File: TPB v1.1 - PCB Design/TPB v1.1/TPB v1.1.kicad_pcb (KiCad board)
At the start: 2 copper layers, 29.5 x 44.7 mm, 28 parts, among them CN1 TYPE-C-31-M-12, J1 Conn_02x03_Top_Bottom, Q1 BC847, Q2 BC847, SW1 SW_Push, SW2 SW_Push, U1 CH340C, U2 AMS1117-3.3

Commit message: PCB Layout v1
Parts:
- C2, C3, R6, R7, U1: moved to B.Cu
- J1: value Conn_02x03_Top_Bottom -> ~
- moved SW2 126.7 mm to (49.2, 175.3), turned to 90 degrees
- moved R5 125.1 mm to (43.4, 180.6), turned to 180 degrees
- moved U1 117.9 mm to (55.8, 172.5), turned to 90 degrees
- moved SW1 116.1 mm to (49.2, 164.9)
- moved R6 111.4 mm to (62.5, 179.0), turned to -90 degrees
- moved R7 110.6 mm to (59.8, 179.0), turned to -90 degrees
- moved R3 110.1 mm to (43.4, 172.6)
- moved R4 105.8 mm to (43.4, 169.5), turned to 180 degrees
- moved Q1 105.6 mm to (43.4, 165.5)
- moved R2 103.5 mm to (43.4, 161.5), turned to 180 degrees
- moved C3 97.5 mm to (59.8, 166.4), turned to 90 degrees
- moved R1 93.1 mm to (48.3, 188.0)
- moved C1 92.4 mm to (48.3, 184.2)
- moved D3 47.5 mm to (43.4, 154.0), turned to 180 degrees
- moved R10 47.4 mm to (43.4, 157.5)
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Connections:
- CN1 pad A6: /USB -> /USB_P
- CN1 pad A7: /USB -> /USB_N
- CN1 pad B6: /USB -> /USB_P
- CN1 pad B7: /USB -> /USB_N
- J1 pad 2: /IO0 -> /TX
- J1 pad 3: GND -> /IO0
- J1 pad 4: /TX -> /RX
- J1 pad 5: /RX -> GND
- U1 pad 5: /USB -> /USB_P
- U1 pad 6: /USB -> /USB_N
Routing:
- net +3V3: track 0.00 -> 103.2 mm, vias 0 -> 7
- net GND: track 23.6 -> 125.8 mm, vias 0 -> 4
- net +5V: track 6.86 -> 62.6 mm, vias 0 -> 2
- net /RTS: track 0.00 -> 46.2 mm, vias 0 -> 1
- net /RX: track 0.00 -> 43.8 mm, vias 0 -> 1
- net /TX: track 0.00 -> 43.6 mm, vias 0 -> 1
- net /EN: track 7.20 -> 39.7 mm
- net /IO0: track 7.20 -> 36.2 mm, vias 0 -> 1
- net /DTR: track 0.00 -> 28.6 mm, vias 0 -> 1
- net Earth: track 0.00 -> 26.4 mm
- net /USB_P: track 0.00 -> 11.2 mm, vias 0 -> 1
- net /USB_N: track 0.00 -> 10.2 mm, vias 0 -> 1
- net Net-(U1-TXD): track 0.00 -> 6.02 mm
- net Net-(Q2-B): track 0.00 -> 4.52 mm
- net Net-(U1-RXD): track 0.00 -> 4.13 mm
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
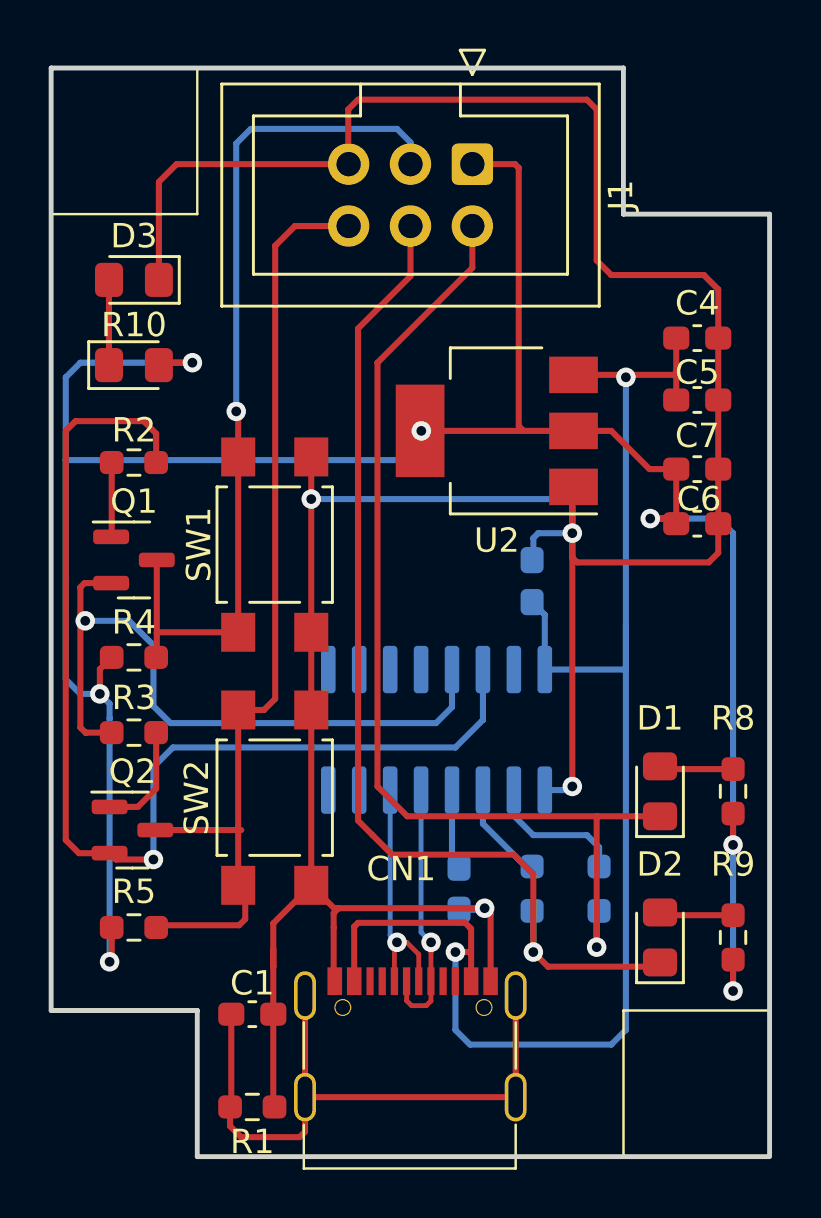
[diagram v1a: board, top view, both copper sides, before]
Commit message: Board Outline, Polygon and 3D of Buttons Added
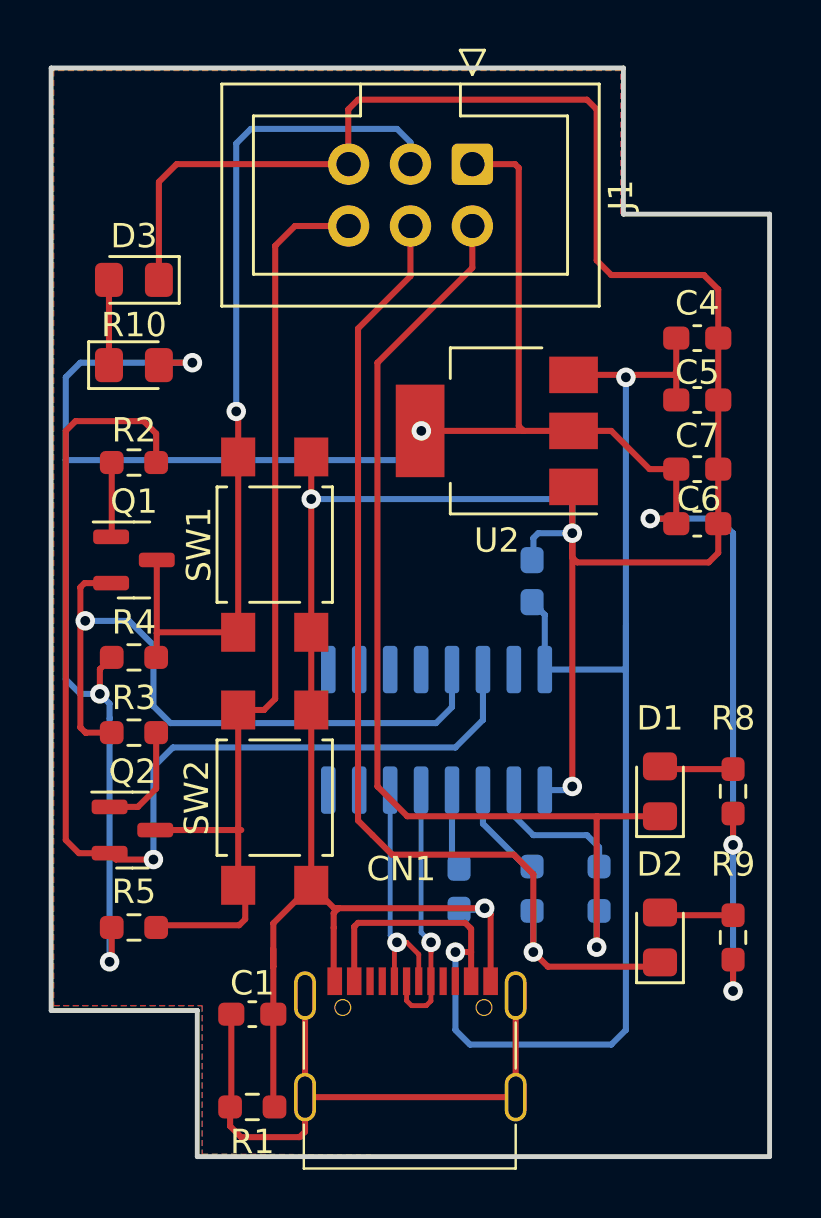
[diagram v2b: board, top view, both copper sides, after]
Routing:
- added copper zone on B.Cu, net GND
- added copper zone on F.Cu, net GND
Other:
- outline, holes or cut-outs redrawn
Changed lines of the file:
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@@
       (layer "B.Paste" (type "Bottom Solder Paste"))
       (layer "B.SilkS" (type "Bottom Silk Screen"))
-      (copper_finish "None")
+      (copper_finish "HAL lead-free")
       (dielectric_constraints no)
+      (edge_connector yes)
     )
     (pad_to_mask_clearance 0)
@@
       (rotate (xyz 0 0 0))
     )
+    (model "${RK_3D}/TL3305AF160QG--3DModel-STEP-520916.STEP"
+      (offset (xyz 0 0 0))
+      (scale (xyz 1 1 1))
+      (rotate (xyz 0 0 0))
+    )
   )
   (footprint "Resistor_SMD:R_0603_1608Metric_Pad0.98x0.95mm_HandSolder" (layer "F.Cu")
@@
     (pad "2" smd rect (at 3.6 1.5 90) (size 1.6 1.4) (layers "F.Cu" "F.Paste" "F.Mask")
       (net 1 "GND") (pinfunction "2") (pintype "passive"))
-    (model "${KICAD6_3DMODEL_DIR}/Button_Switch_SMD.3dshapes/SW_SPST_TL3305C.wrl"
+    (model "${KICAD6_3DMODEL_DIR}/Button_Switch_SMD.3dshapes/SW_SPST_TL3305C.wrl" hide
+      (offset (xyz 0 0 0))
+      (scale (xyz 1 1 1))
+      (rotate (xyz 0 0 0))
+    )
+    (model "${RK_3D}/TL3305AF160QG--3DModel-STEP-520916.STEP"
       (offset (xyz 0 0 0))
       (scale (xyz 1 1 1))
@@
     (fp_line (start 4.7 11.8) (end -4 11.8)
       (stroke (width 0.1) (type default)) (layer "F.SilkS"))
-    (pad "" np_thru_hole circle (at -2.4 5.19) (size 0.7 0.7) (drill oval 0.6) (layers "F&B.Cu" "*.Mask"))
-    (pad "" np_thru_hole circle (at 3.4 5.19) (size 0.7 0.7) (drill oval 0.6) (layers "F&B.Cu" "*.Mask"))
+    (pad "" np_thru_hole circle (at -2.4 5.19) (size 0.7 0.7) (drill oval 0.6) (layers "*.Cu" "*.Mask"))
+    (pad "" np_thru_hole circle (at 3.4 5.19) (size 0.7 0.7) (drill oval 0.6) (layers "*.Cu" "*.Mask"))
     (pad "A1/B12" smd trapezoid (at -2.73 4.11) (size 0.6 1.14) (layers "F.Cu" "F.Paste" "F.Mask")
       (net 1 "GND") (pinfunction "GND") (pintype "power_in") (thermal_bridge_angle 45))
@@
     )
   )
-  (gr_rect (start 40 145.3) (end 46 151.3)
-    (stroke (width 0.1) (type default)) (fill none) (layer "F.SilkS"))
-  (gr_rect (start 63.5 184) (end 69.5 190)
-    (stroke (width 0.1) (type default)) (fill none) (layer "F.SilkS"))
   (gr_line (start 40 184) (end 40 145.3)
     (stroke (width 0.2) (type default)) (layer "Edge.Cuts"))
   (gr_line (start 63.5 145.3) (end 40 145.3)
     (stroke (width 0.2) (type default)) (layer "Edge.Cuts"))
-  (gr_line (start 69.5 151.3) (end 69.5 189.9)
+  (gr_line (start 69.5 151.3) (end 69.5 190)
     (stroke (width 0.2) (type default)) (layer "Edge.Cuts"))
   (gr_line (start 40 184) (end 46 184)
@@
   (segment (start 53.92 180.92) (end 53.92 174.95) (width 0.2) (layer "B.Cu") (net 31))
   (segment (start 54.2 181.2) (end 53.92 180.92) (width 0.2) (layer "B.Cu") (net 31))
+  (zone (net 1) (net_name "GND") (layers "F&B.Cu") (name "GND") (hatch none 0.5)
+    (connect_pads (clearance 0.5))
+    (min_thickness 0.25) (filled_areas_thickness no)
+    (fill yes (thermal_gap 0.5) (thermal_bridge_width 0.5) (island_removal_mode 1) (island_area_min 10))
+    (polygon
+      (pts
+        (xy 69.5 190)
+        (xy 69.5 151.3)
+        (xy 63.4 151.3)
+        (xy 63.4 145.4)
+        (xy 40.1 145.4)
+        (xy 40.1 183.8)
+        (xy 46.2 183.8)
+        (xy 46.2 189.9)
+      )
+    )
+  )
 )

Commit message: Pcb Design Complated
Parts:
- added G***: LOGO, RK_Graphics:RK_Logo_10x10mm, F.Cu at (58.3, 169.7)
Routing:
- net +3V3: track 103.2 -> 103.7 mm, vias 7 -> 12
- net GND: vias 4 -> 28
- added copper zone on B.Cu, net +3V3
- added copper zone on F.Cu, net +3V3
- added copper zone on F.Cu, net +5V
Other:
- board text added: "3V3"
- board text added: "EN"
- board text added: "GND"
- board text added: "IO0"
- board text added: "RX"
- board text added: "TPB v1.1"
- board text added: "TX"

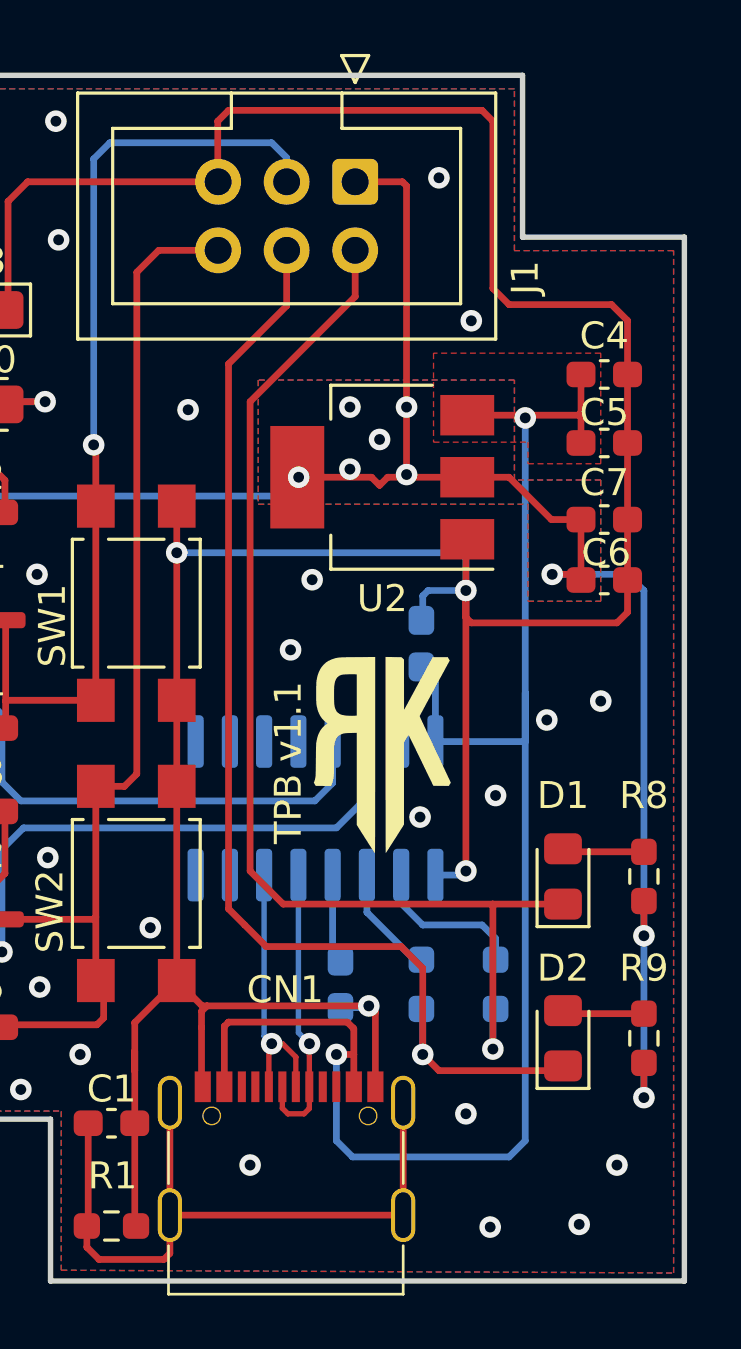
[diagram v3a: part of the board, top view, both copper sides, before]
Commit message: DRC Errs Solved
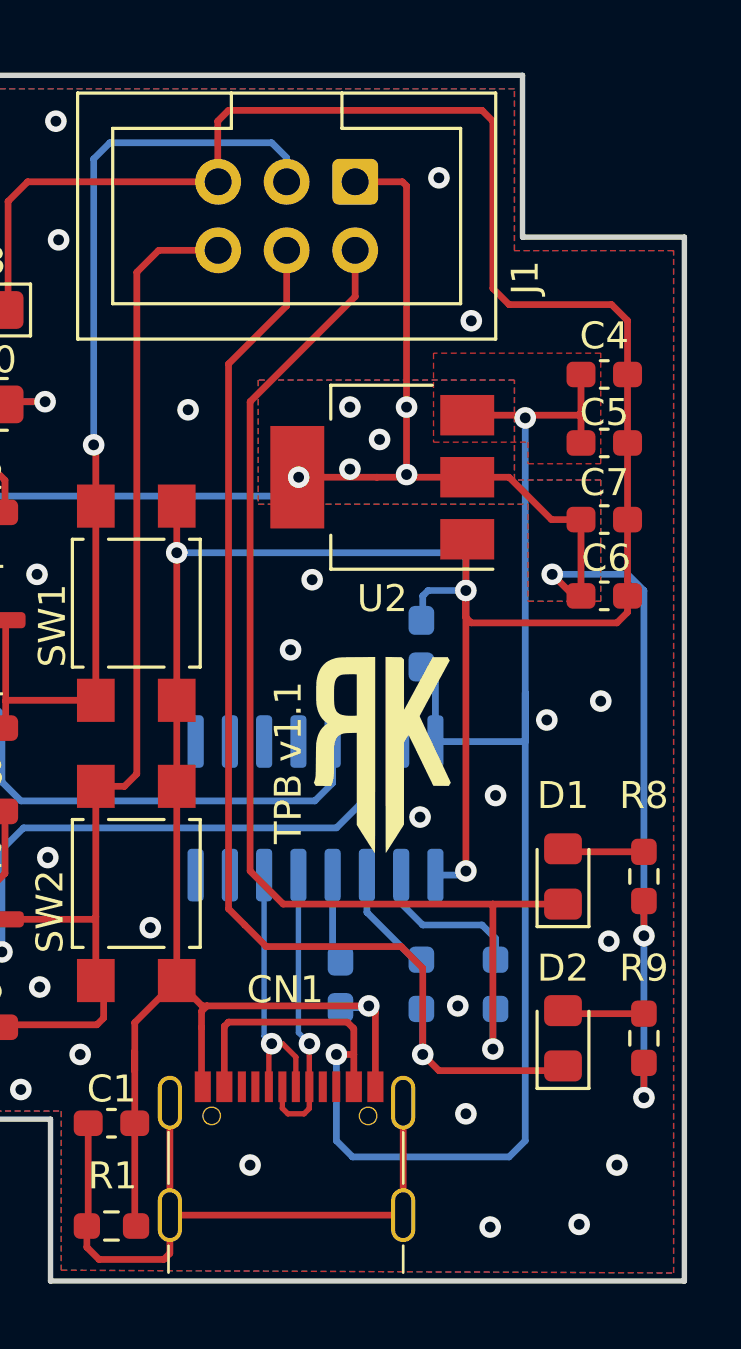
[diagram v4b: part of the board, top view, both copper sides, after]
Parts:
- moved C6 0.59 mm to (66.5, 164.6)
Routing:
- net +3V3: track 103.7 -> 104.3 mm
- net GND: vias 28 -> 30
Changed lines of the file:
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@@
         (effects (font (size 1 1) (thickness 0.15)))
     )
-    (fp_line (start -4.68 -0.5) (end -4.68 0.5)
-      (stroke (width 0.12) (type solid)) (layer "F.SilkS"))
-    (fp_line (start -4.68 0.5) (end -3.68 0)
-      (stroke (width 0.12) (type solid)) (layer "F.SilkS"))
-    (fp_line (start -3.68 0) (end -4.68 -0.5)
-      (stroke (width 0.12) (type solid)) (layer "F.SilkS"))
     (fp_line (start -3.29 -5.21) (end 5.83 -5.21)
       (stroke (width 0.12) (type solid)) (layer "F.SilkS"))
@@
   )
   (footprint "Capacitor_SMD:C_0603_1608Metric_Pad1.08x0.95mm_HandSolder" (layer "F.Cu")
-    (at 66.53 164.01)
+    (at 66.53 164.6)
     (descr "Capacitor SMD 0603 (1608 Metric), square (rectangular) end terminal, IPC_7351 nominal with elongated pad for handsoldering. (Body size source: IPC-SM-782 page 76, https://www.pcb-3d.com/wordpress/wp-content/uploads/ipc-sm-782a_amendment_1_and_2.pdf), generated with kicad-footprint-generator")
     (tags "capacitor handsolder")
@@
     (property "ki_keywords" "cap capacitor")
     (attr smd)
-    (fp_text reference "C6" (at 0.07 -1.01) (layer "F.SilkS")
+    (fp_text reference "C6" (at 0.07 -1.4) (layer "F.SilkS")
         (effects (font (size 1 1) (thickness 0.15)))
     )
@@
     (fp_line (start -4 7.7) (end -4 5.8)
       (stroke (width 0.1) (type default)) (layer "F.SilkS"))
-    (fp_line (start -4 11.8) (end -4 10)
+    (fp_line (start -4 11) (end -4 10)
       (stroke (width 0.1) (type default)) (layer "F.SilkS"))
     (fp_line (start 4.7 5.8) (end 4.7 7.7)
       (stroke (width 0.1) (type default)) (layer "F.SilkS"))
-    (fp_line (start 4.7 10) (end 4.7 11.8)
-      (stroke (width 0.1) (type default)) (layer "F.SilkS"))
-    (fp_line (start 4.7 11.3) (end -4 11.3)
-      (stroke (width 0.1) (type default)) (layer "F.SilkS"))
-    (fp_line (start 4.7 11.8) (end -4 11.8)
+    (fp_line (start 4.7 10) (end 4.7 11)
       (stroke (width 0.1) (type default)) (layer "F.SilkS"))
     (pad "" np_thru_hole circle (at -2.4 5.19) (size 0.7 0.7) (drill oval 0.6) (layers "*.Cu" "*.Mask"))
@@
     (pts (xy 63.5 145.2) (xy 63.5 151.2))
     (height -10.5)
-    (gr_text "6.0000 mm" (at 72.85 148.2 90) (layer "Dwgs.User")
+    (gr_text "236.2205 mils" (at 72.85 148.2 90) (layer "Dwgs.User")
       (effects (font (size 1 1) (thickness 0.15)))
     )
@@
     (pts (xy 69.5 151.2) (xy 63.5 151.2))
     (height 8.4)
-    (gr_text "6.0000 mm" (at 66.5 141.65) (layer "Dwgs.User")
+    (gr_text "236.2205 mils" (at 66.5 141.65) (layer "Dwgs.User")
       (effects (font (size 1 1) (thickness 0.15)))
     )
@@
     (pts (xy 69.5 151.2) (xy 69.5 189.9))
     (height -10.5)
-    (gr_text "38.7000 mm" (at 78.85 170.55 90) (layer "Dwgs.User")
+    (gr_text "1523.6220 mils" (at 78.85 170.55 90) (layer "Dwgs.User")
       (effects (font (size 1 1) (thickness 0.15)))
     )
@@
   (via (at 47.1 181.6) (size 0.8) (drill 0.4) (layers "F.Cu" "B.Cu") (free) (net 1))
   (via (at 60.4 149.1) (size 0.8) (drill 0.4) (layers "F.Cu" "B.Cu") (free) (net 1))
+  (via (at 66.7 177.4) (size 0.8) (drill 0.4) (layers "F.Cu" "B.Cu") (free) (net 1))
   (via (at 67 185.7) (size 0.8) (drill 0.4) (layers "F.Cu" "B.Cu") (free) (net 1))
   (via (at 54.9 166.6) (size 0.8) (drill 0.4) (layers "F.Cu" "B.Cu") (free) (net 1))
@@
   (via (at 46.3 151.4) (size 0.8) (drill 0.4) (layers "F.Cu" "B.Cu") (free) (net 1))
   (via (at 59.7 172.8) (size 0.8) (drill 0.4) (layers "F.Cu" "B.Cu") (free) (net 1))
+  (via (at 61.1 179.8) (size 0.8) (drill 0.4) (layers "F.Cu" "B.Cu") (free) (net 1))
   (via (at 46.2 147) (size 0.8) (drill 0.4) (layers "F.Cu" "B.Cu") (free) (net 1))
   (via (at 64.4 169.2) (size 0.8) (drill 0.4) (layers "F.Cu" "B.Cu") (free) (net 1))
@@
   (segment (start 59.075 183.387313) (end 59.075 187.557313) (width 0.25) (layer "F.Cu") (net 2))
   (segment (start 47.3975 184.15) (end 47.3975 187.91) (width 0.25) (layer "F.Cu") (net 2))
-  (segment (start 65.4575 163.8) (end 65.6675 164.01) (width 0.25) (layer "F.Cu") (net 3))
-  (segment (start 57.9 160.2) (end 55.15 160.2) (width 0.25) (layer "F.Cu") (net 3))
-  (segment (start 58.5 160.2) (end 58.2 160.5) (width 0.25) (layer "F.Cu") (net 3))
+  (segment (start 65.4 164.6) (end 64.6 163.8) (width 0.25) (layer "F.Cu") (net 3))
   (segment (start 42.41 180.59) (end 42.4 180.6) (width 0.25) (layer "F.Cu") (net 3))
   (segment (start 45.8 157.4) (end 44.525 157.4) (width 0.25) (layer "F.Cu") (net 3))
   (segment (start 68 181.9125) (end 68 183.2) (width 0.25) (layer "F.Cu") (net 3))
   (segment (start 44.525 157.4) (end 44.425 157.5) (width 0.25) (layer "F.Cu") (net 3))
-  (segment (start 58.2 160.5) (end 57.9 160.2) (width 0.25) (layer "F.Cu") (net 3))
+  (segment (start 58.1 160.2) (end 55.15 160.2) (width 0.25) (layer "F.Cu") (net 3))
   (segment (start 61.45 160.2) (end 59.4 160.2) (width 0.25) (layer "F.Cu") (net 3))
   (segment (start 42 171) (end 42 169.9875) (width 0.25) (layer "F.Cu") (net 3))
-  (segment (start 65.6675 161.77) (end 65.6675 164.01) (width 0.25) (layer "F.Cu") (net 3))
   (segment (start 59.2 160) (end 59.4 160.2) (width 0.25) (layer "F.Cu") (net 3))
   (segment (start 42.4875 180.59) (end 42.4875 181.9125) (width 0.25) (layer "F.Cu") (net 3))
-  (segment (start 64.6 163.8) (end 65.4575 163.8) (width 0.25) (layer "F.Cu") (net 3))
   (segment (start 59.2 149.4) (end 59.2 160) (width 0.25) (layer "F.Cu") (net 3))
+  (segment (start 59.4 160.2) (end 58.1 160.2) (width 0.25) (layer "F.Cu") (net 3))
   (segment (start 57.295 149.2475) (end 59.0475 149.2475) (width 0.25) (layer "F.Cu") (net 3))
   (segment (start 68 177.2) (end 68 175.9125) (width 0.25) (layer "F.Cu") (net 3))
@@
   (segment (start 42 169.9875) (end 42.4875 169.5) (width 0.25) (layer "F.Cu") (net 3))
   (segment (start 59.0475 149.2475) (end 59.2 149.4) (width 0.25) (layer "F.Cu") (net 3))
-  (segment (start 59.4 160.2) (end 58.5 160.2) (width 0.25) (layer "F.Cu") (net 3))
+  (segment (start 65.6675 161.77) (end 65.6675 164.6) (width 0.25) (layer "F.Cu") (net 3))
+  (segment (start 65.6675 164.6) (end 65.4 164.6) (width 0.25) (layer "F.Cu") (net 3))
   (via (at 42.4 182) (size 0.8) (drill 0.4) (layers "F.Cu" "B.Cu") (net 3))
   (via (at 57.1 159.9) (size 0.8) (drill 0.4) (layers "F.Cu" "B.Cu") (free) (net 3))
@@
     (connect_pads (clearance 0.4))
     (min_thickness 0.4) (filled_areas_thickness no)
-    (fill yes (thermal_gap 0.4) (thermal_bridge_width 0.4) (smoothing fillet) (radius 2) (island_removal_mode 1) (island_area_min 10))
+    (fill yes (thermal_gap 0.4) (thermal_bridge_width 0.4) (smoothing fillet) (radius 2))
     (polygon
       (pts
